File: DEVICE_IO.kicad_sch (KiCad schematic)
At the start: 3 parts, among them J5 CAM_0, J6 CAM_1, J7 47080-4005

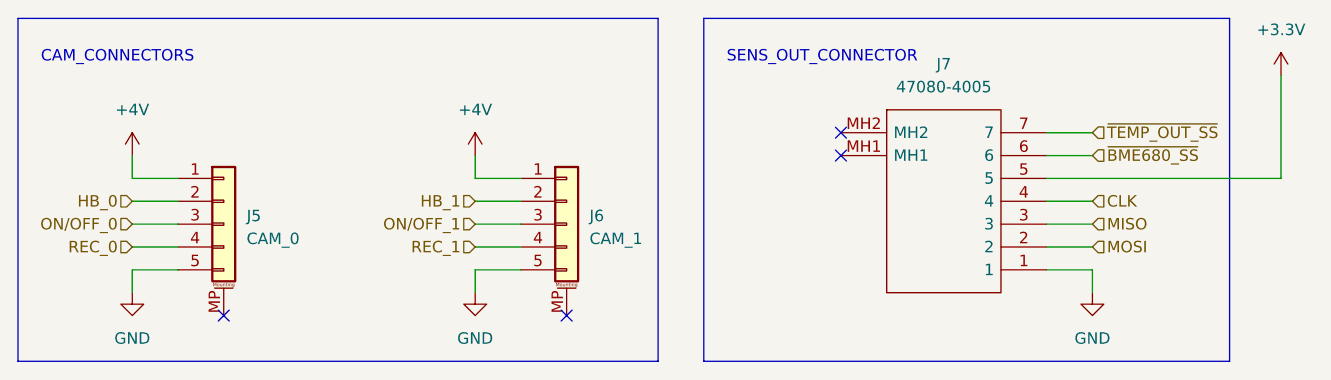
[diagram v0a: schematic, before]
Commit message: V1
- Corrected SD-cards footprint and schematical represantation;
- Corrected RTC shematics:
	- changed oscilators power supply from internal 3v3 to Vbat so RTC works when PCB is disconnected from external power supply [PWR PCB];
	- 32 kHz to microcontroller now comes from RTC module;
	- added 100 nF decoupling capacitor to Vbat RTC pin.
- Corrected couple connections and component placement on PCB
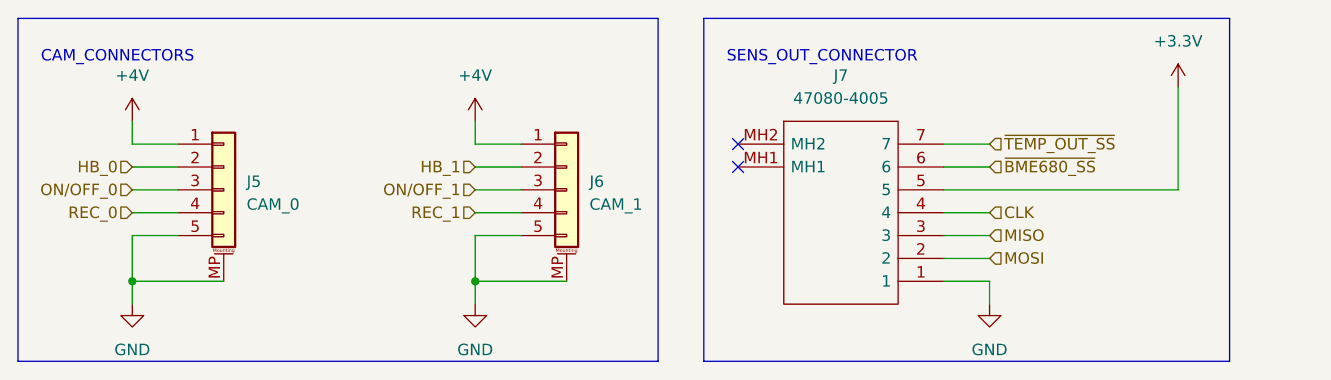
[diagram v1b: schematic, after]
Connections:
- net GND: now also J5.MP (MountPin), J6.MP (MountPin)
- no-connect marks 4 -> 2
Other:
- company: (none) -> BASEMENT
- moved on the sheet: J5, J6, J7
